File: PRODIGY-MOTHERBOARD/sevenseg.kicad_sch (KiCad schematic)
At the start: 2 parts, among them U14 MAX7219 / tm1637, U15 CC56-12YWA

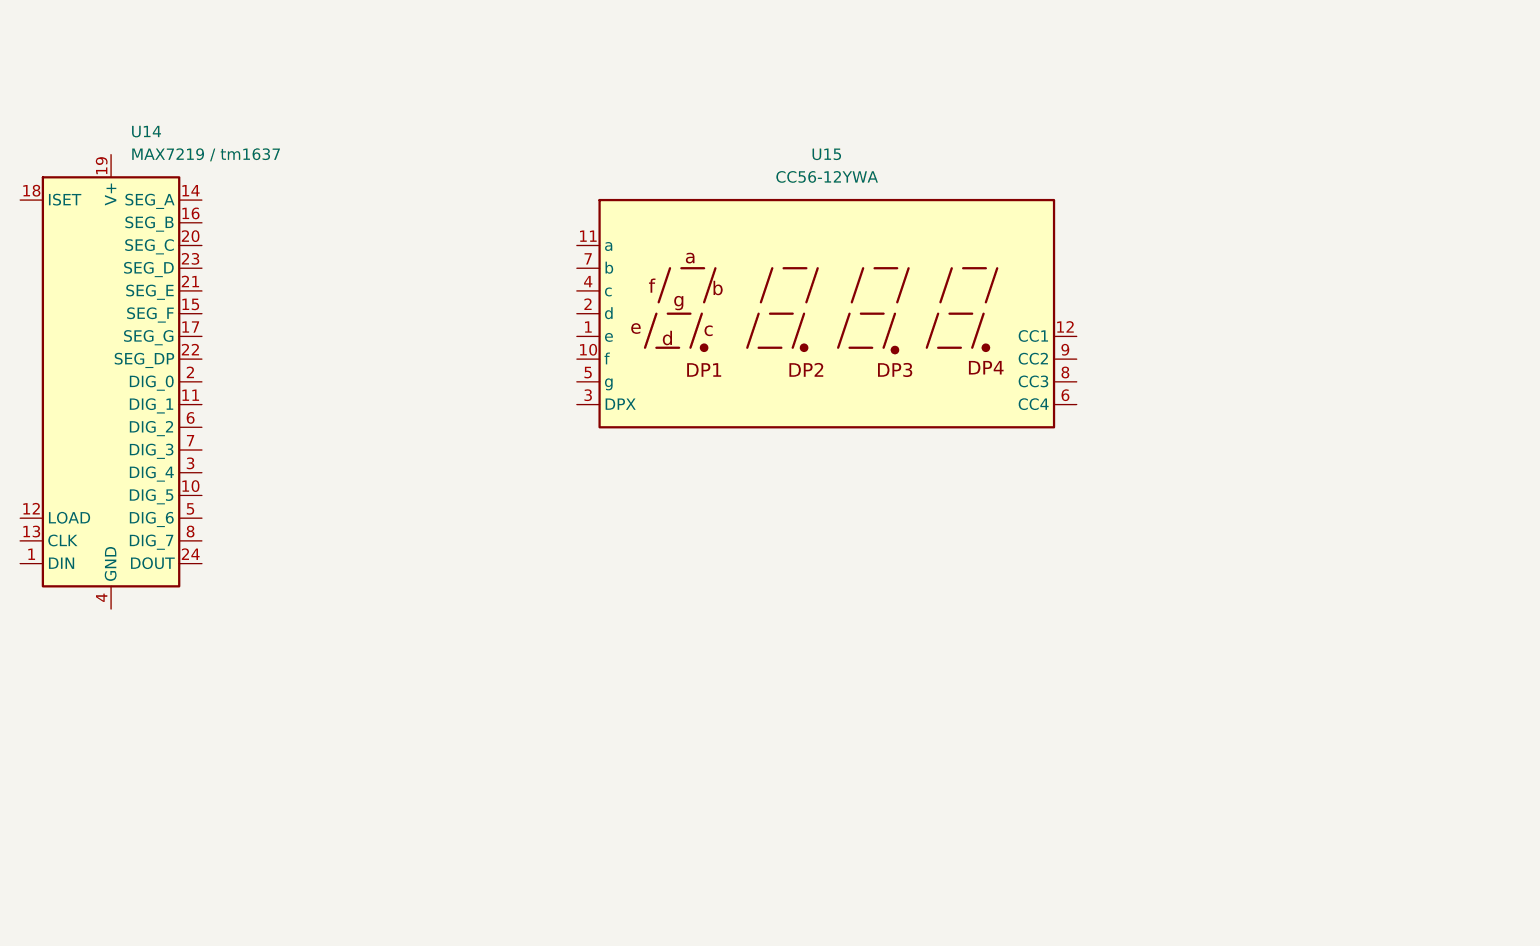
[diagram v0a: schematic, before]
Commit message: Finished I2C device and bus schematics. Added logic level translation.
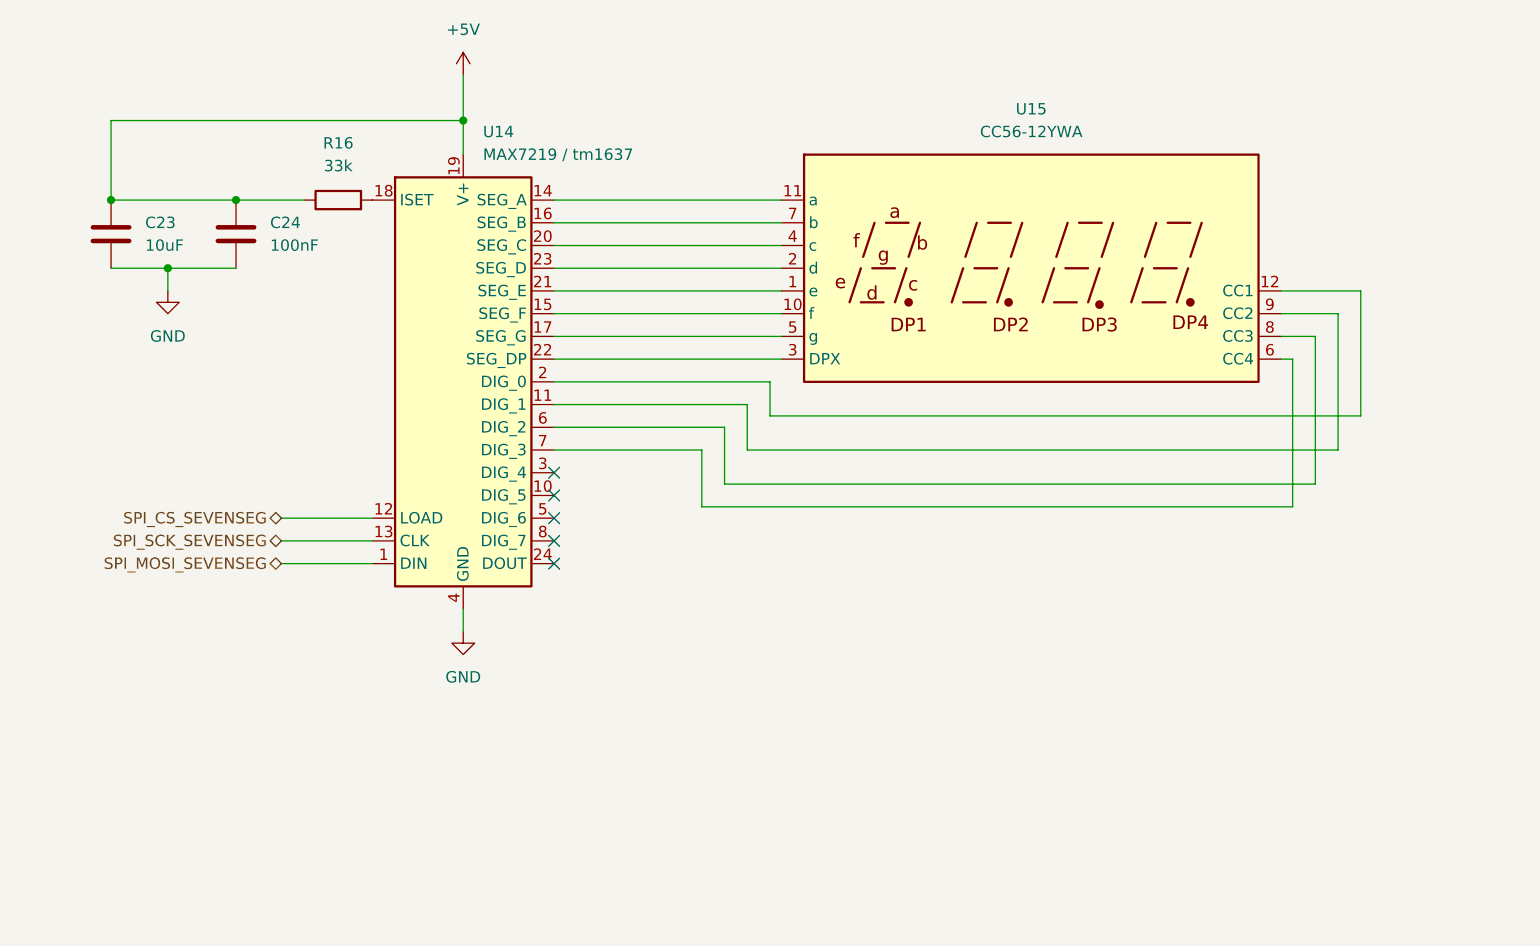
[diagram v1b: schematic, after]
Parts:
- added C23: 10uF, Capacitor_SMD:C_0805_2012Metric, symbol Device:C
- added C24: 100nF, Capacitor_SMD:C_0603_1608Metric, symbol Device:C
- added R16: 33k, Resistor_SMD:R_0603_1608Metric, symbol Device:R
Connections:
- net at U15.1 (e): now also U14.21 (SEG_E)
- net at U15.10 (f): now also U14.15 (SEG_F)
- net at U15.11 (a): now also U14.14 (SEG_A)
- net at U15.12 (CC1): now also U14.2 (DIG_0)
- net at U15.2 (d): now also U14.23 (SEG_D)
- net at U15.3 (DPX): now also U14.22 (SEG_DP)
- net at U15.4 (c): now also U14.20 (SEG_C)
- net at U15.5 (g): now also U14.17 (SEG_G)
- net at U15.6 (CC4): now also U14.7 (DIG_3)
- net at U15.7 (b): now also U14.16 (SEG_B)
- net at U15.8 (CC3): now also U14.6 (DIG_2)
- net at U15.9 (CC2): now also U14.11 (DIG_1)
- net SPI_MOSI_SEVENSEG: now reaches U14.1 (DIN)
- net SPI_CS_SEVENSEG: now reaches U14.12 (LOAD)
- net SPI_SCK_SEVENSEG: now reaches U14.13 (CLK)
- net at U14.18 (ISET): now also R16.2
- net +5V: now reaches U14.19 (V+)
- net +5V: now also C23.1, C24.1, R16.1
- net GND: now reaches U14.4 (GND), U14.9 (GND)
- net GND: now also C23.2, C24.2
- no-connect marks 0 -> 5
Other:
- moved on the sheet: U14, U15

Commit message: CAN schematic done
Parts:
- renumbered C23 to C2, C24 to C3, R16 to R5, U14 to U1, U15 to U2
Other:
- moved on the sheet: U2

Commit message: Added proper debounce filter elements to buttons.
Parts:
- renumbered U2 to U1, U1 to U2
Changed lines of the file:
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@@
 		(dnp no)
 		(fields_autoplaced yes)
-		(property "Reference" "U2"
+		(property "Reference" "U1"
 			(at 185.42 36.83 0)
 			(effects
@@
 			(project "PRODIGY-MOTHERBOARD"
 				(path "/f1c25860-8989-4190-bd24-2491d23ca7d9/e2913798-f444-47a6-8b64-53020d7d816b/5b2ed776-5334-4587-8715-0b58b66b66ac"
-					(reference "U2")
+					(reference "U1")
 					(unit 1)
 				)
@@
 		(dnp no)
 		(fields_autoplaced yes)
-		(property "Reference" "U1"
+		(property "Reference" "U2"
 			(at 119.0341 39.37 0)
 			(effects
@@
 			(project "PRODIGY-MOTHERBOARD"
 				(path "/f1c25860-8989-4190-bd24-2491d23ca7d9/e2913798-f444-47a6-8b64-53020d7d816b/5b2ed776-5334-4587-8715-0b58b66b66ac"
-					(reference "U1")
+					(reference "U2")
 					(unit 1)
 				)
@@
 		(dnp no)
 		(fields_autoplaced yes)
-		(property "Reference" "#PWR09"
+		(property "Reference" "#PWR011"
 			(at 83.82 63.5 0)
 			(effects
@@
 			(project "PRODIGY-MOTHERBOARD"
 				(path "/f1c25860-8989-4190-bd24-2491d23ca7d9/e2913798-f444-47a6-8b64-53020d7d816b/5b2ed776-5334-4587-8715-0b58b66b66ac"
-					(reference "#PWR09")
+					(reference "#PWR011")
 					(unit 1)
 				)
@@
 		(dnp no)
 		(fields_autoplaced yes)
-		(property "Reference" "#PWR011"
+		(property "Reference" "#PWR012"
 			(at 116.84 101.6 0)
 			(effects
@@
 			(project "PRODIGY-MOTHERBOARD"
 				(path "/f1c25860-8989-4190-bd24-2491d23ca7d9/e2913798-f444-47a6-8b64-53020d7d816b/5b2ed776-5334-4587-8715-0b58b66b66ac"
-					(reference "#PWR011")
-					(unit 1)
-				)
+					(reference "#PWR012")
+					(unit 1)
+				)

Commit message: Submitted V0 for evaluation. Avaiting feedback.
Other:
- note added: "Can be removed, but it's a nice addition 1 digit display could be broken out (7 pins with no dpx) To be directly controlled by MCU (breakout pins)"
- moved on the sheet: U1
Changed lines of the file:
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@@
 	(wire
 		(pts
-			(xy 127 74.93) (xy 148.59 74.93)
-		)
-		(stroke
-			(width 0)
-			(type default)
-		)
-	)
-	(wire
-		(pts
-			(xy 156.21 71.12) (xy 222.25 71.12)
-		)
-		(stroke
-			(width 0)
-			(type default)
-		)
-	)
-	(wire
-		(pts
-			(xy 157.48 62.23) (xy 127 62.23)
+			(xy 127 74.93) (xy 135.89 74.93)
+		)
+		(stroke
+			(width 0)
+			(type default)
+		)
+	)
+	(wire
+		(pts
+			(xy 143.51 71.12) (xy 209.55 71.12)
+		)
+		(stroke
+			(width 0)
+			(type default)
+		)
+	)
+	(wire
+		(pts
+			(xy 144.78 62.23) (xy 127 62.23)
 		)
 		(stroke
@@
 	(wire
 		(pts
-			(xy 217.17 78.74) (xy 217.17 62.23)
-		)
-		(stroke
-			(width 0)
-			(type default)
-		)
-	)
-	(wire
-		(pts
-			(xy 151.13 72.39) (xy 151.13 78.74)
+			(xy 204.47 78.74) (xy 204.47 62.23)
+		)
+		(stroke
+			(width 0)
+			(type default)
+		)
+	)
+	(wire
+		(pts
+			(xy 138.43 72.39) (xy 138.43 78.74)
 		)
 		(stroke
@@
 	(wire
 		(pts
-			(xy 157.48 49.53) (xy 127 49.53)
-		)
-		(stroke
-			(width 0)
-			(type default)
-		)
-	)
-	(wire
-		(pts
-			(xy 217.17 62.23) (xy 213.36 62.23)
+			(xy 144.78 49.53) (xy 127 49.53)
+		)
+		(stroke
+			(width 0)
+			(type default)
+		)
+	)
+	(wire
+		(pts
+			(xy 204.47 62.23) (xy 200.66 62.23)
 		)
 		(stroke
@@
 	(wire
 		(pts
-			(xy 214.63 64.77) (xy 213.36 64.77)
+			(xy 201.93 64.77) (xy 200.66 64.77)
 		)
 		(stroke
@@
 	(wire
 		(pts
-			(xy 156.21 67.31) (xy 156.21 71.12)
-		)
-		(stroke
-			(width 0)
-			(type default)
-		)
-	)
-	(wire
-		(pts
-			(xy 213.36 59.69) (xy 219.71 59.69)
-		)
-		(stroke
-			(width 0)
-			(type default)
-		)
-	)
-	(wire
-		(pts
-			(xy 222.25 71.12) (xy 222.25 57.15)
+			(xy 143.51 67.31) (xy 143.51 71.12)
+		)
+		(stroke
+			(width 0)
+			(type default)
+		)
+	)
+	(wire
+		(pts
+			(xy 200.66 59.69) (xy 207.01 59.69)
+		)
+		(stroke
+			(width 0)
+			(type default)
+		)
+	)
+	(wire
+		(pts
+			(xy 209.55 71.12) (xy 209.55 57.15)
 		)
 		(stroke
@@
 	(wire
 		(pts
-			(xy 151.13 78.74) (xy 217.17 78.74)
-		)
-		(stroke
-			(width 0)
-			(type default)
-		)
-	)
-	(wire
-		(pts
-			(xy 157.48 59.69) (xy 127 59.69)
-		)
-		(stroke
-			(width 0)
-			(type default)
-		)
-	)
-	(wire
-		(pts
-			(xy 157.48 57.15) (xy 127 57.15)
-		)
-		(stroke
-			(width 0)
-			(type default)
-		)
-	)
-	(wire
-		(pts
-			(xy 219.71 74.93) (xy 219.71 59.69)
-		)
-		(stroke
-			(width 0)
-			(type default)
-		)
-	)
-	(wire
-		(pts
-			(xy 214.63 81.28) (xy 214.63 64.77)
-		)
-		(stroke
-			(width 0)
-			(type default)
-		)
-	)
-	(wire
-		(pts
-			(xy 127 67.31) (xy 156.21 67.31)
+			(xy 138.43 78.74) (xy 204.47 78.74)
+		)
+		(stroke
+			(width 0)
+			(type default)
+		)
+	)
+	(wire
+		(pts
+			(xy 144.78 59.69) (xy 127 59.69)
+		)
+		(stroke
+			(width 0)
+			(type default)
+		)
+	)
+	(wire
+		(pts
+			(xy 144.78 57.15) (xy 127 57.15)
+		)
+		(stroke
+			(width 0)
+			(type default)
+		)
+	)
+	(wire
+		(pts
+			(xy 207.01 74.93) (xy 207.01 59.69)
+		)
+		(stroke
+			(width 0)
+			(type default)
+		)
+	)
+	(wire
+		(pts
+			(xy 201.93 81.28) (xy 201.93 64.77)
+		)
+		(stroke
+			(width 0)
+			(type default)
+		)
+	)
+	(wire
+		(pts
+			(xy 127 67.31) (xy 143.51 67.31)
 		)
 		(stroke
@@
 	(wire
 		(pts
-			(xy 153.67 69.85) (xy 153.67 74.93)
+			(xy 140.97 69.85) (xy 140.97 74.93)
 		)
 		(stroke
@@
 	(wire
 		(pts
-			(xy 127 72.39) (xy 151.13 72.39)
-		)
-		(stroke
-			(width 0)
-			(type default)
-		)
-	)
-	(wire
-		(pts
-			(xy 148.59 74.93) (xy 148.59 81.28)
+			(xy 127 72.39) (xy 138.43 72.39)
+		)
+		(stroke
+			(width 0)
+			(type default)
+		)
+	)
+	(wire
+		(pts
+			(xy 135.89 74.93) (xy 135.89 81.28)
 		)
 		(stroke
@@
 	(wire
 		(pts
-			(xy 127 69.85) (xy 153.67 69.85)
-		)
-		(stroke
-			(width 0)
-			(type default)
-		)
-	)
-	(wire
-		(pts
-			(xy 148.59 81.28) (xy 214.63 81.28)
+			(xy 127 69.85) (xy 140.97 69.85)
+		)
+		(stroke
+			(width 0)
+			(type default)
+		)
+	)
+	(wire
+		(pts
+			(xy 135.89 81.28) (xy 201.93 81.28)
 		)
 		(stroke
@@
 	(wire
 		(pts
-			(xy 157.48 54.61) (xy 127 54.61)
-		)
-		(stroke
-			(width 0)
-			(type default)
-		)
-	)
-	(wire
-		(pts
-			(xy 157.48 46.99) (xy 127 46.99)
-		)
-		(stroke
-			(width 0)
-			(type default)
-		)
-	)
-	(wire
-		(pts
-			(xy 222.25 57.15) (xy 213.36 57.15)
-		)
-		(stroke
-			(width 0)
-			(type default)
-		)
-	)
-	(wire
-		(pts
-			(xy 157.48 52.07) (xy 127 52.07)
-		)
-		(stroke
-			(width 0)
-			(type default)
-		)
-	)
-	(wire
-		(pts
-			(xy 157.48 64.77) (xy 127 64.77)
+			(xy 144.78 54.61) (xy 127 54.61)
+		)
+		(stroke
+			(width 0)
+			(type default)
+		)
+	)
+	(wire
+		(pts
+			(xy 144.78 46.99) (xy 127 46.99)
+		)
+		(stroke
+			(width 0)
+			(type default)
+		)
+	)
+	(wire
+		(pts
+			(xy 209.55 57.15) (xy 200.66 57.15)
+		)
+		(stroke
+			(width 0)
+			(type default)
+		)
+	)
+	(wire
+		(pts
+			(xy 144.78 52.07) (xy 127 52.07)
+		)
+		(stroke
+			(width 0)
+			(type default)
+		)
+	)
+	(wire
+		(pts
+			(xy 144.78 64.77) (xy 127 64.77)
 		)
 		(stroke
@@
 	(wire
 		(pts
-			(xy 153.67 74.93) (xy 219.71 74.93)
-		)
-		(stroke
-			(width 0)
-			(type default)
+			(xy 140.97 74.93) (xy 207.01 74.93)
+		)
+		(stroke
+			(width 0)
+			(type default)
+		)
+	)
+	(text "Can be removed, but it's a nice addition\n\n1 digit display \ncould be broken out\n(7 pins with no dpx)\nTo be directly controlled\nby MCU (breakout pins)"
+		(exclude_from_sim no)
+		(at 136.144 112.268 0)
+		(effects
+			(font
+				(size 2.54 2.54)
+				(thickness 0.508)
+				(bold yes)
+			)
+			(justify left bottom)
 		)
 	)
@@
 	(symbol
 		(lib_id "Display_Character:CC56-12SEKWA")
-		(at 185.42 54.61 0)
+		(at 172.72 54.61 0)
 		(unit 1)
 		(exclude_from_sim no)
@@
 		(fields_autoplaced yes)
 		(property "Reference" "U1"
-			(at 185.42 36.83 0)
+			(at 172.72 36.83 0)
 			(effects
 				(font
@@
 		)
 		(property "Value" "CC56-12YWA"
-			(at 185.42 39.37 0)
+			(at 172.72 39.37 0)
 			(effects
 				(font
@@
 		)
 		(property "Footprint" "Display_7Segment:CC56-12YWA"
-			(at 185.42 69.85 0)
+			(at 172.72 69.85 0)
 			(effects
 				(font
@@
 		)
 		(property "Datasheet" "http://www.kingbright.com/attachments/file/psearch/000/00/00/CC56-12SEKWA(Ver.7A).pdf"
-			(at 174.498 53.848 0)
+			(at 161.798 53.848 0)
 			(effects
 				(font
@@
 		)
 		(property "Description" "4 digit 7 segment super bright orange LED, common cathode"
-			(at 185.42 54.61 0)
-			(effects
-				(font
+			(at 172.72 54.61 0)
+			(effects
+				(font

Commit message: Finished v0.1 schematic.
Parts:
- renumbered C2 to C42, C3 to C43, R5 to R32, U2 to U14, U1 to U15
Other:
- note removed: "Can be removed, but it's a nice addition 1 digit display could be broken out (7 pins with no dpx) To be directly controlled by MCU (breakout pins)"
- moved on the sheet: C42, C43, R32, U14, U15

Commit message: schematic v0.2 finalized
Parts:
- renumbered C42 to C41, C43 to C42
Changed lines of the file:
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@@
 		(dnp no)
 		(fields_autoplaced yes)
-		(property "Reference" "C43"
+		(property "Reference" "C42"
 			(at 101.6 76.1999 0)
 			(effects
@@
 			(project "PRODIGY-MOTHERBOARD"
 				(path "/f1c25860-8989-4190-bd24-2491d23ca7d9/e2913798-f444-47a6-8b64-53020d7d816b/5b2ed776-5334-4587-8715-0b58b66b66ac"
-					(reference "C43")
+					(reference "C42")
 					(unit 1)
 				)
@@
 		(dnp no)
 		(fields_autoplaced yes)
-		(property "Reference" "#PWR0144"
+		(property "Reference" "#PWR0148"
 			(at 123.19 63.5 0)
 			(effects
@@
 			(project "PRODIGY-MOTHERBOARD"
 				(path "/f1c25860-8989-4190-bd24-2491d23ca7d9/e2913798-f444-47a6-8b64-53020d7d816b/5b2ed776-5334-4587-8715-0b58b66b66ac"
-					(reference "#PWR0144")
+					(reference "#PWR0148")
 					(unit 1)
 				)
@@
 		(dnp no)
 		(fields_autoplaced yes)
-		(property "Reference" "#PWR0143"
+		(property "Reference" "#PWR0147"
 			(at 90.17 90.17 0)
 			(effects
@@
 			(project "PRODIGY-MOTHERBOARD"
 				(path "/f1c25860-8989-4190-bd24-2491d23ca7d9/e2913798-f444-47a6-8b64-53020d7d816b/5b2ed776-5334-4587-8715-0b58b66b66ac"
-					(reference "#PWR0143")
+					(reference "#PWR0147")
 					(unit 1)
 				)
@@
 		(dnp no)
 		(fields_autoplaced yes)
-		(property "Reference" "C42"
+		(property "Reference" "C41"
 			(at 87.63 76.1999 0)
 			(effects
@@
 			(project "PRODIGY-MOTHERBOARD"
 				(path "/f1c25860-8989-4190-bd24-2491d23ca7d9/e2913798-f444-47a6-8b64-53020d7d816b/5b2ed776-5334-4587-8715-0b58b66b66ac"
-					(reference "C42")
+					(reference "C41")
 					(unit 1)
 				)
@@
 		(dnp no)
 		(fields_autoplaced yes)
-		(property "Reference" "#PWR0145"
+		(property "Reference" "#PWR0149"
 			(at 123.19 128.27 0)
 			(effects
@@
 			(project "PRODIGY-MOTHERBOARD"
 				(path "/f1c25860-8989-4190-bd24-2491d23ca7d9/e2913798-f444-47a6-8b64-53020d7d816b/5b2ed776-5334-4587-8715-0b58b66b66ac"
-					(reference "#PWR0145")
-					(unit 1)
-				)
+					(reference "#PWR0149")
+					(unit 1)
+				)

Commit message: Motherboard footprints assigned.
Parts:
- U14: footprint (none) -> Package_SO:SOIC-24W_7.5x15.4mm_P1.27mm
- U15: footprint Display_7Segment:CC56-12YWA -> Display_7Segment:CA56-12SRWA; TME (none) -> FYQ-3641AUHR-21
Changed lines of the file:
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@@
+			)
+		)
+		(property "MOUSER" ""
+			(at 109.22 73.66 0)
+			(effects
+				(font
+					(size 1.27 1.27)
+				)
+				(hide yes)
+			)
+		)
+		(property "Sim.Type" ""
+			(at 109.22 73.66 0)
+			(effects
+				(font
+					(size 1.27 1.27)
+				)
+				(hide yes)
+			)
+		)
+		(property "TME" ""
+			(at 109.22 73.66 0)
+			(effects
+				(font
+					(size 1.27 1.27)
+				)
+				(hide yes)
 			)
 		)
@@
 			)
 		)
-		(property "Footprint" "Display_7Segment:CC56-12YWA"
+		(property "Footprint" "Display_7Segment:CA56-12SRWA"
 			(at 180.34 96.52 0)
 			(effects
@@
 		)
 		(property "Description" "4 digit 7 segment super bright orange LED, common cathode"
+			(at 180.34 81.28 0)
+			(effects
+				(font
+					(size 1.27 1.27)
+				)
+				(hide yes)
+			)
+		)
+		(property "MOUSER" ""
+			(at 180.34 81.28 0)
+			(effects
+				(font
+					(size 1.27 1.27)
+				)
+				(hide yes)
+			)
+		)
+		(property "Sim.Type" ""
+			(at 180.34 81.28 0)
+			(effects
+				(font
+					(size 1.27 1.27)
+				)
+				(hide yes)
+			)
+		)
+		(property "TME" "FYQ-3641AUHR-21"
 			(at 180.34 81.28 0)
 			(effects
@@
 			)
 		)
-		(property "Footprint" ""
+		(property "Footprint" "Package_SO:SOIC-24W_7.5x15.4mm_P1.27mm"
 			(at 121.92 92.71 0)
 			(effects
@@
 		)
 		(property "Description" "8-Digit LED Display Driver"
+			(at 123.19 93.98 0)
+			(effects
+				(font
+					(size 1.27 1.27)
+				)
+				(hide yes)
+			)
+		)
+		(property "MOUSER" ""
+			(at 123.19 93.98 0)
+			(effects
+				(font
+					(size 1.27 1.27)
+				)
+				(hide yes)
+			)
+		)
+		(property "Sim.Type" ""
+			(at 123.19 93.98 0)
+			(effects
+				(font
+					(size 1.27 1.27)
+				)
+				(hide yes)
+			)
+		)
+		(property "TME" ""
 			(at 123.19 93.98 0)
 			(effects
@@
 			)
 		)
+		(property "MOUSER" ""
+			(at 97.79 77.47 0)
+			(effects
+				(font
+					(size 1.27 1.27)
+				)
+				(hide yes)
+			)
+		)
+		(property "Sim.Type" ""
+			(at 97.79 77.47 0)
+			(effects
+				(font
+					(size 1.27 1.27)
+				)
+				(hide yes)
+			)
+		)
+		(property "TME" ""
+			(at 97.79 77.47 0)
+			(effects
+				(font
+					(size 1.27 1.27)
+				)
+				(hide yes)
+			)
+		)
 		(pin "1"
 		)
@@
 			(at 83.82 77.47 0)
 			(effects
+				(font
+					(size 1.27 1.27)
+				)
+				(hide yes)
+			)
+		)
+		(property "MOUSER" ""
+			(at 83.82 77.47 0)
+			(effects
+				(font
+					(size 1.27 1.27)
+				)
+				(hide yes)
+			)
+		)
+		(property "Sim.Type" ""
+			(at 83.82 77.47 0)
+			(effects
+				(font
+					(size 1.27 1.27)
+				)
+				(hide yes)
+			)
+		)
+		(property "TME" ""
+			(at 83.82 77.47 0)
+			(effects

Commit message: finished motherboard bom and updated footprints
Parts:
- C41: TME (none) -> CL21A106KOQNNNE
- C42: TME (none) -> CL10B104KB8NNNC
- R32: TME (none) -> ERJ3EKF3302V
- U14: TME (none) -> MAX7219CWG+
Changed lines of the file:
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@@
 			)
 		)
-		(property "TME" ""
+		(property "TME" "ERJ3EKF3302V"
 			(at 109.22 73.66 0)
 			(effects
@@
 			)
 		)
-		(property "TME" ""
+		(property "TME" "MAX7219CWG+"
 			(at 123.19 93.98 0)
 			(effects
@@
 			)
 		)
-		(property "TME" ""
+		(property "TME" "CL10B104KB8NNNC  "
 			(at 97.79 77.47 0)
 			(effects
@@
 			)
 		)
-		(property "TME" ""
+		(property "TME" "CL21A106KOQNNNE  "
 			(at 83.82 77.47 0)
 			(effects
